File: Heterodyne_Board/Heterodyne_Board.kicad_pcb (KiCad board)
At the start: 2 copper layers, 57.4 x 69.5 mm, 57 parts, among them J1 AVR-ISP-6, J2 Speaker, J3 SWITCH, J4 LED, J6 AudioJack2_Ground_Switch, J7 Barrel_Jack, SW1 SW_SPST, SW2 SW_SPST, U1 ATtiny85-20P, U2 TLV9054xD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

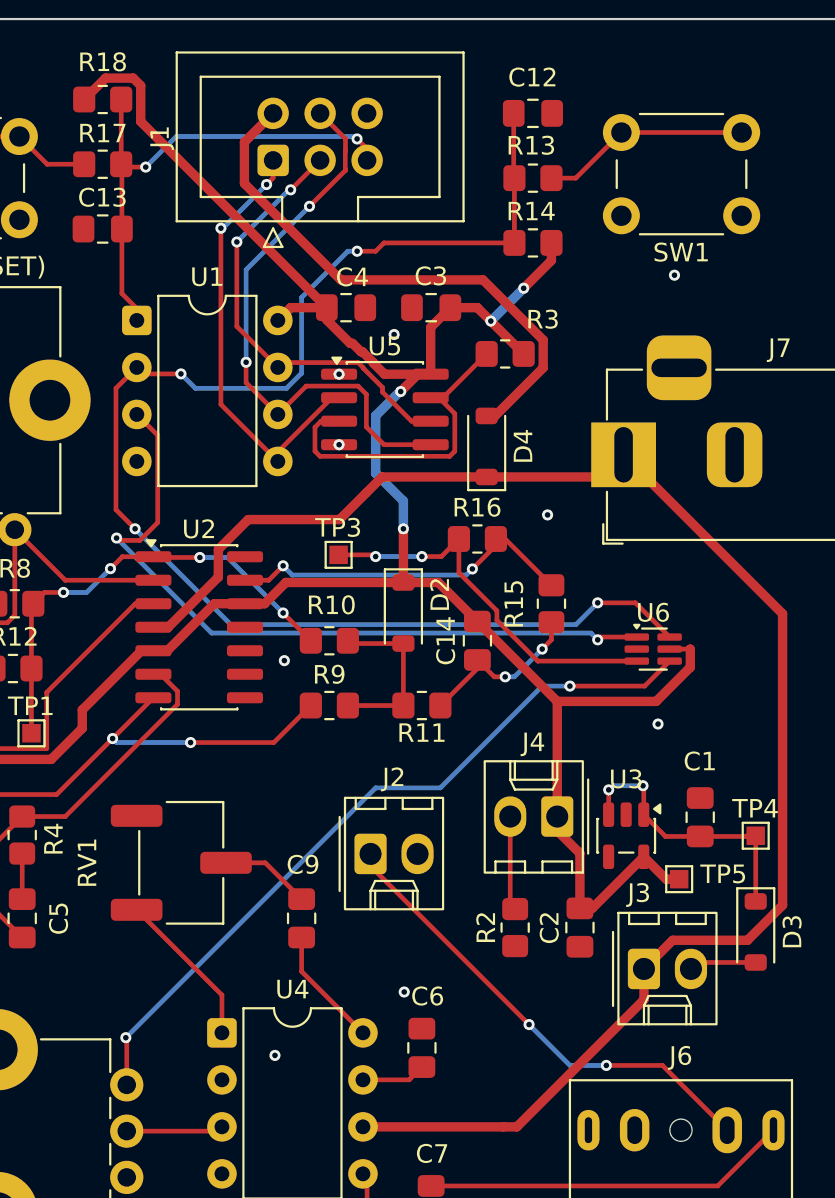
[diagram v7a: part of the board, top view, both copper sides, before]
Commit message: fixed routing on switch chip
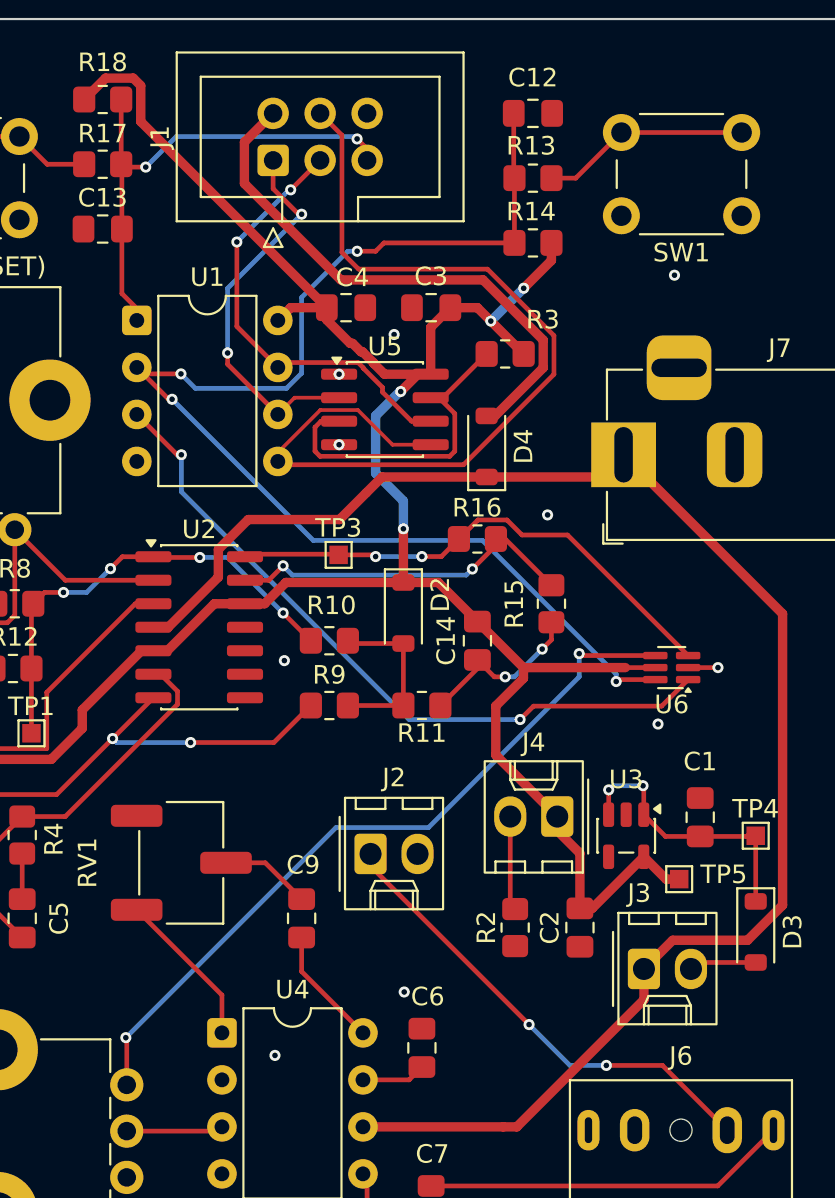
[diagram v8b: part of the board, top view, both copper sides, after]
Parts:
- moved U6 1.41 mm to (184.0, 95.5), turned to 180 degrees
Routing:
- net /MOSI: track 31.0 -> 50.9 mm, vias 2 -> 0
- net /Mixer_Out: track 20.6 -> 27.9 mm
- net /Audio_EN: track 75.8 -> 69.2 mm
- net /MISO: track 23.8 -> 20.9 mm
- net +3V3: track 149.8 -> 148.1 mm
- net GND: track 2.91 -> 4.52 mm, vias 11 -> 12
- net /MCU_Out: track 39.4 -> 38.7 mm
